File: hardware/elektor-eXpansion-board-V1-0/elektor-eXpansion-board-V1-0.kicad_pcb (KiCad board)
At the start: 2 copper layers, 62.2 x 43.7 mm, 30 parts, among them J1 IO1, J10 5V-GND, J11 Qwiic, J12 Qwiic, J13 5442219, J2 IO3, J3 IO4, J4 IO2, J5 I2C.., J6 I2C.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

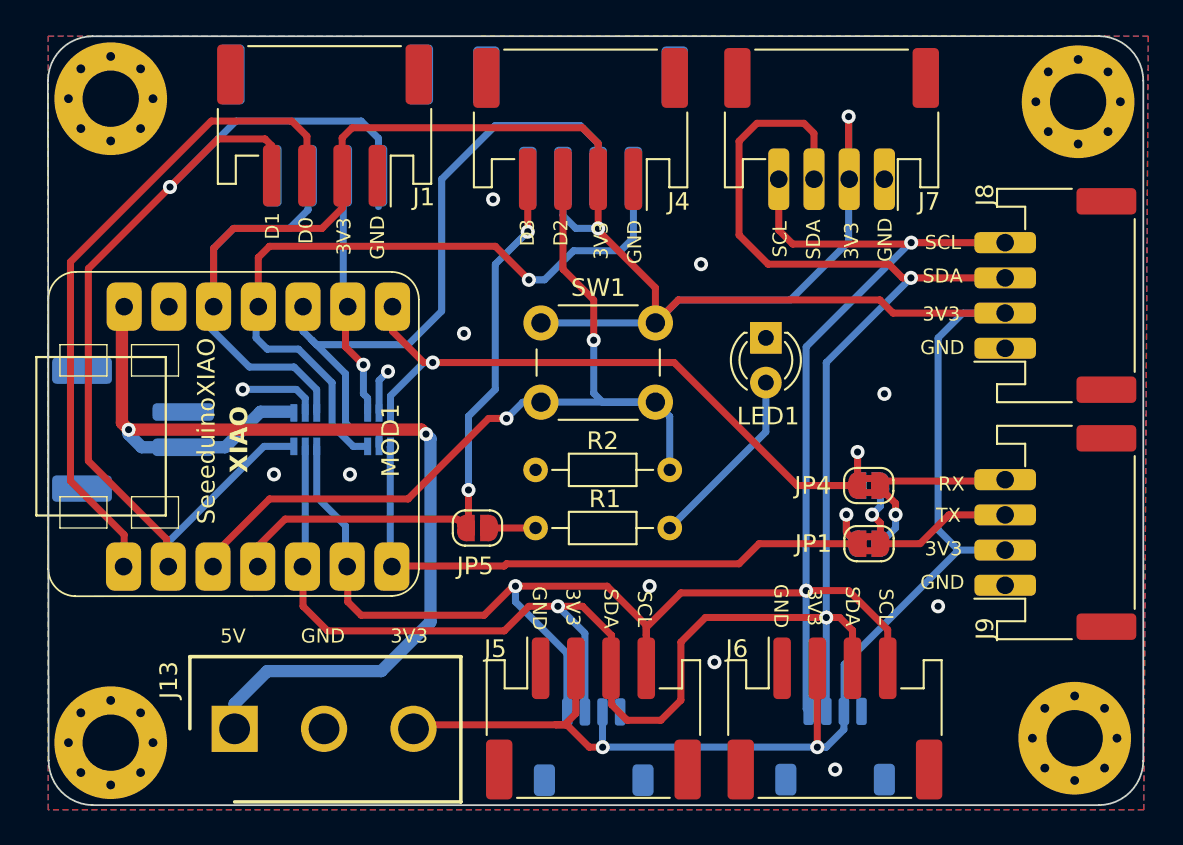
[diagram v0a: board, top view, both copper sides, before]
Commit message: v1.01
feat: Release v1.01 of Elektor eXpansion Board

- Improved overall PCB layout for better performance and usability.
- Enhanced Xiao board footprint to support both SMD and THT soldering.
- Optimized power, I2C, and UART track routing for improved signal integrity.
- Adjusted placement of button and LED for better accessibility.
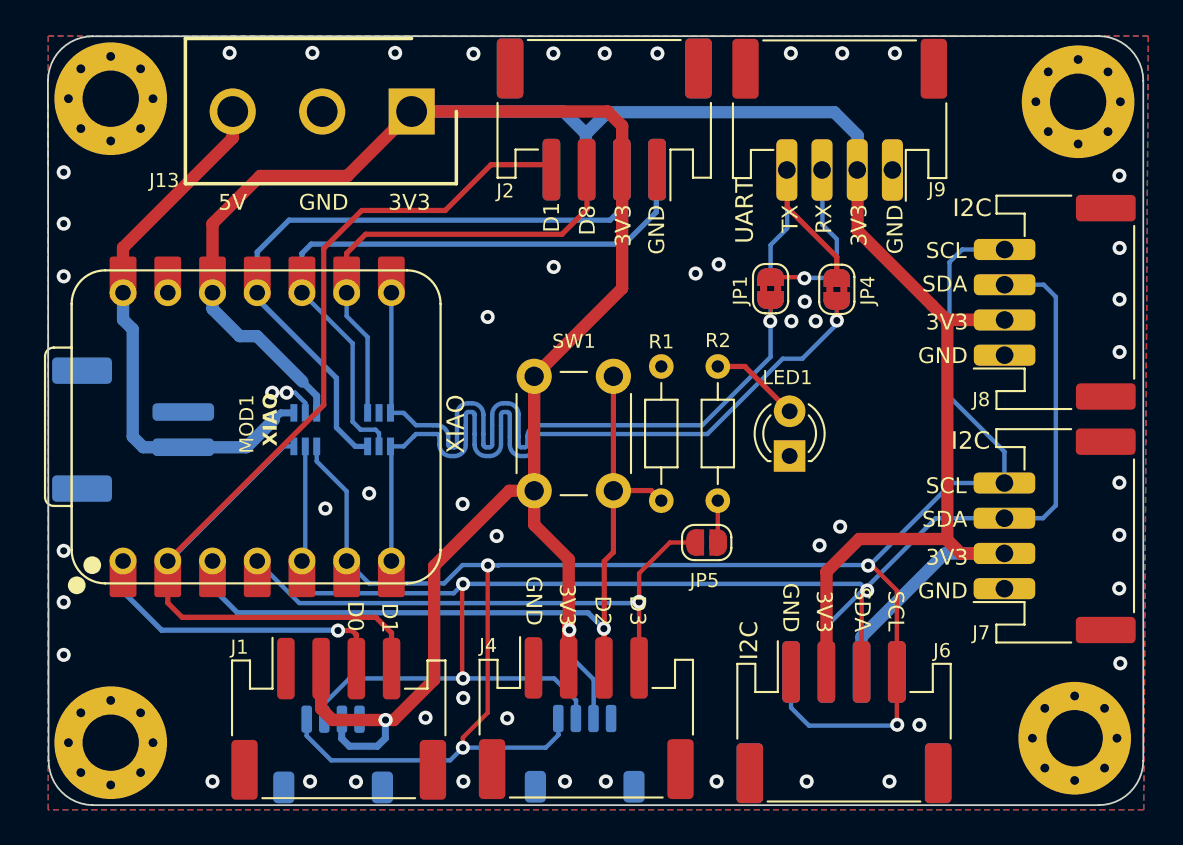
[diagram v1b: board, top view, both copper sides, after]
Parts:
- removed the G*** at (156.2, 62.2)
- added G***: LOGO, footprints:elektorlabs-20x6.1mm, B.Cu at (148.6, 59.8)
- J2: moved to F.Cu
- J5: moved to B.Cu
- MOD1: footprint footprints:Seeeduino XIAO-MOUDLE14P-2.54-21X17.8MM -> lib:XIAO-ESP32C3-DIP
- moved J13 36.5 mm to (138.0, 34.0), turned to 180 degrees
- moved J1 33.7 mm to (133.9, 68.5), turned to 0 degrees
- moved J4 33.5 mm to (147.9, 68.5), turned to 0 degrees
- moved J12 28.5 mm to (133.5, 70.5)
- moved J9 26.4 mm to (162.3, 34.5), turned to 180 degrees
- moved J7 26.4 mm to (174.5, 58.1), turned to 90 degrees
- moved J2 15.8 mm to (148.9, 34.5), turned to 180 degrees
- moved JP1 15.5 mm to (158.4, 44.1), turned to 90 degrees
- moved JP2 15.5 mm to (158.4, 44.1), turned to 90 degrees
- moved J5 14.2 mm to (162.5, 68.7), turned to 180 degrees
- moved MOD1 13.8 mm to (129.2, 51.8)
- moved JP5 13.0 mm to (154.8, 58.5)
- moved JP3 11.3 mm to (162.1, 44.1), turned to 90 degrees
- moved JP4 11.3 mm to (162.1, 44.1), turned to 90 degrees
- moved R1 10.5 mm to (155.4, 56.1), turned to 90 degrees
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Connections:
- D2 pad 3: D7 -> UART_N
- D2 pad 4: TXD -> UART_P
- J1 pad MP: GND -> unconnected-(J1-MountPin-PadMP)
- J11 pad MP: GND -> unconnected-(J11-MountPin-PadMP)_1
- J12 pad MP: GND -> unconnected-(J12-MountPin-PadMP)_1
- J13 pad 1: +5V -> +3V3
- J13 pad 3: +3V3 -> +5V
- J2 pad MP: GND -> unconnected-(J2-MountPin-PadMP)
- J3 pad 3: D9 -> D10
- J3 pad 4: D10 -> D9
- J3 pad MP: GND -> unconnected-(J3-MountPin-PadMP)_1
- J4 pad MP: GND -> unconnected-(J4-MountPin-PadMP)_1
- J5 pad MP: GND -> unconnected-(J5-MountPin-PadMP)
- J6 pad MP: GND -> unconnected-(J6-MountPin-PadMP)
- J7 pad MP: GND -> unconnected-(J7-MountPin-PadMP)
- J8 pad MP: GND -> unconnected-(J8-MountPin-PadMP)
- J9 pad MP: GND -> unconnected-(J9-MountPin-PadMP)
- JP1 pad 1: TXD -> UART_N
- JP2 pad 1: TXD -> UART_N
- JP3 pad 1: D7 -> UART_P
- JP4 pad 1: D7 -> UART_P
- MOD1 pad 7: TXD -> UART_P
- MOD1 pad 8: D7 -> UART_N
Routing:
- net UART_P: track 0.00 -> 47.8 mm, vias 0 -> 1
- net UART_N: track 0.00 -> 45.2 mm, vias 0 -> 1
- net D7: track 40.3 -> 0.00 mm, vias 2 -> 0
- net TXD: track 38.3 -> 0.00 mm, vias 1 -> 0
- net +5V: track 60.9 -> 30.6 mm, vias 2 -> 0
- net D0: track 38.4 -> 18.3 mm, vias 0 -> 1
- net +3V3: track 187.5 -> 200.9 mm, vias 4 -> 2
- net D8: track 14.1 -> 25.9 mm, vias 1 -> 0
- net SDA: track 115.2 -> 103.7 mm
- net SCL: track 102.1 -> 111.2 mm, vias 3 -> 4
- net Net-(LED1-A): track 10.5 -> 5.13 mm
- net GND: track 7.52 -> 2.75 mm, vias 12 -> 52
- net D3: track 35.6 -> 32.0 mm, vias 2 -> 1
- net D10: track 41.7 -> 38.2 mm, vias 1 -> 0
- net D2: track 50.9 -> 47.7 mm, vias 2 -> 1
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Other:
- board text added: "I2C"
- board text added: "UART"
- board text added: "XIAO"
- board text added: "eXpansion Board v1.01"
- board text removed: "eXpansion Board V1.0"
